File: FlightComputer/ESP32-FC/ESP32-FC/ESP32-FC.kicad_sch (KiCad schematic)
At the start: 19 parts, among them J1 USB_C_Receptacle_USB2.0_16P, U1 ESP32-S3-WROOM-1, U2 AP2112K-3.3, U3 ICP-20100, U4 ICM-42670-P

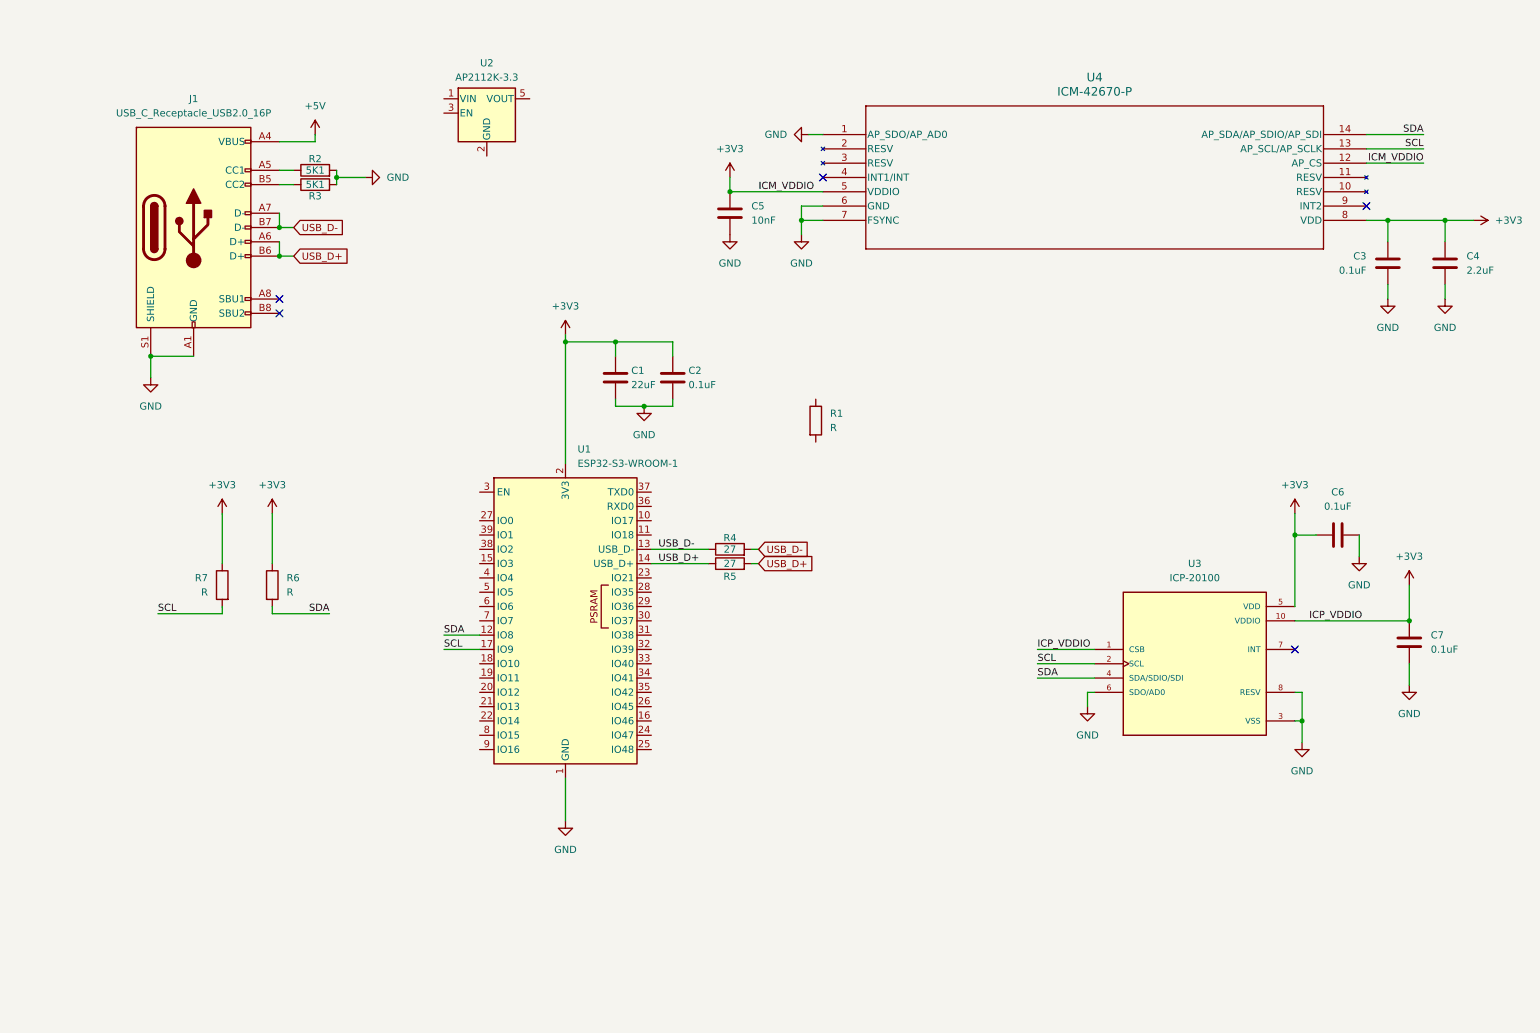
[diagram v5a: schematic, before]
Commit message: Updated power architecture
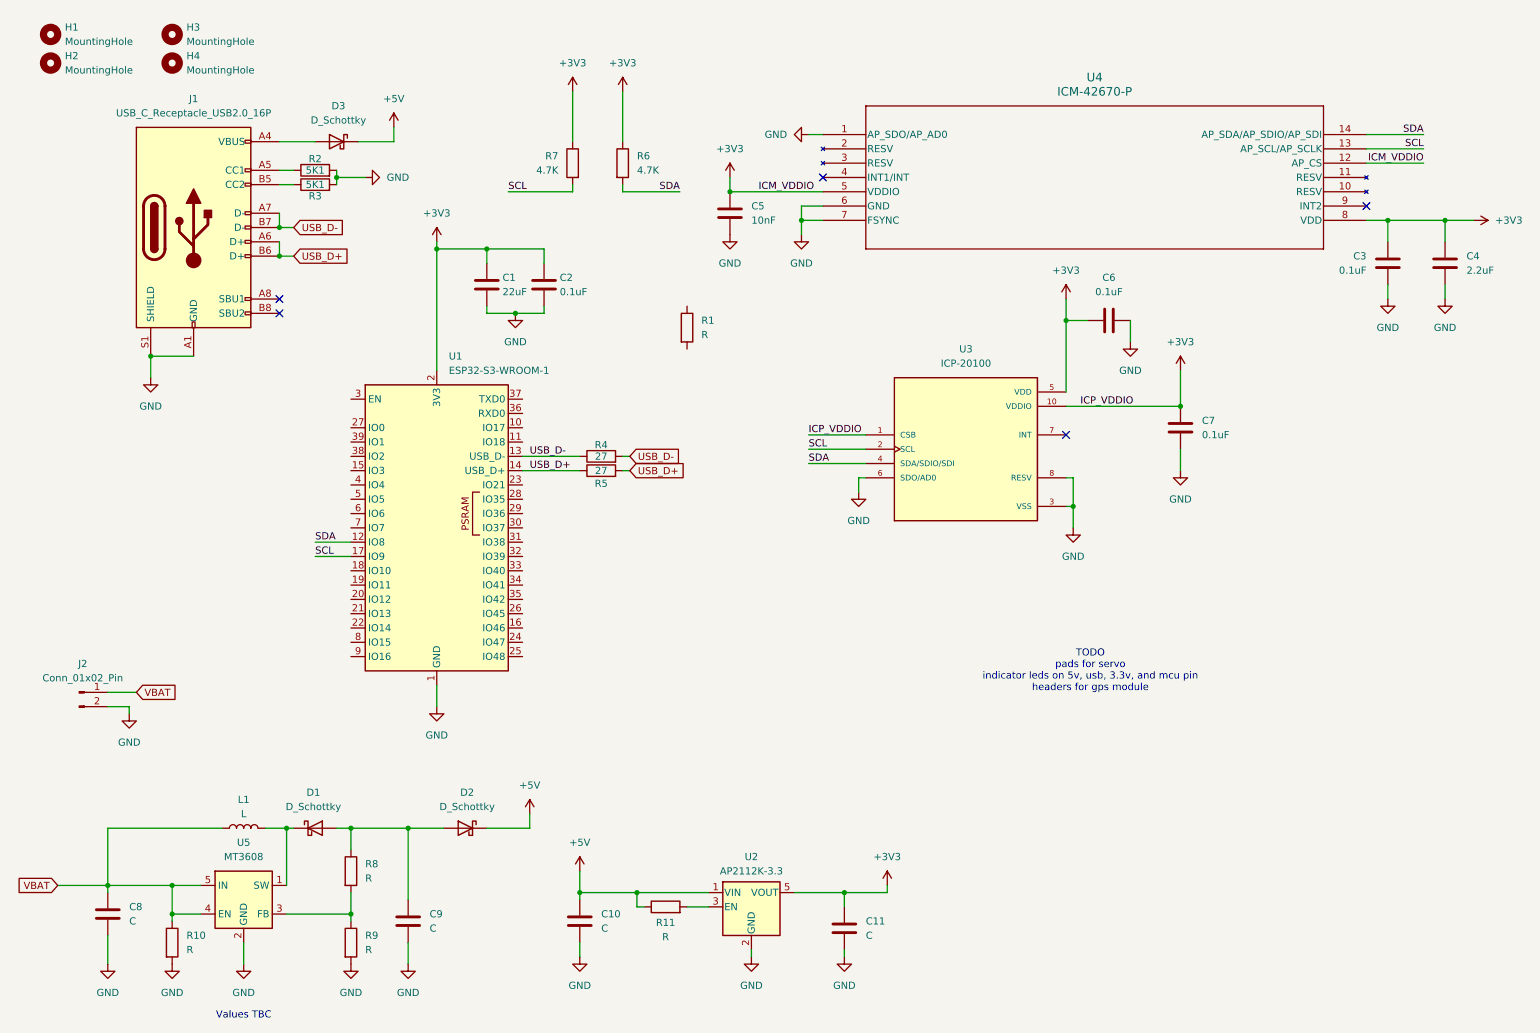
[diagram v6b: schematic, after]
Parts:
- added C10, C11, C8, C9: C, symbol Device:C
- added D1, D2, D3: D_Schottky, symbol Device:D_Schottky
- added H1, H2, H3, H4: MountingHole, symbol Mechanical:MountingHole
- added J2: Conn_01x02_Pin, symbol Connector:Conn_01x02_Pin
- added L1: L, symbol Device:L
- added R10, R11, R8, R9: R, symbol Device:R
- added U5: MT3608, Package_TO_SOT_SMD:SOT-23-6, symbol Regulator_Switching:MT3608
- R6, R7: value R -> 4.7K
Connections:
- net +3V3: now also U2.5 (VOUT), C11.1
- net +5V: now also U2.1 (VIN), C10.1, D2.1 (K), D3.1 (K), R11.1; no longer J1.A4 (VBUS), J1.A9 (VBUS), J1.B4 (VBUS), J1.B9 (VBUS)
- net GND: now also U2.2 (GND), C10.2, C11.2, C8.2, C9.2, J2.2 (Pin_2), R10.2, R9.2, U5.2 (GND)
- net at U2.3 (EN): now also R11.2
- new net: D3.2 (A), J1.A4 (VBUS), J1.A9 (VBUS), J1.B4 (VBUS), J1.B9 (VBUS)
- new net: D1.1 (K), L1.2, U5.1 (SW)
- new net: R8.2, R9.1, U5.3 (FB)
- new net: C9.1, D1.2 (A), D2.2 (A), R8.1
- new net VBAT: C8.1, J2.1 (Pin_1), L1.1, R10.1, U5.4 (EN), U5.5 (IN)
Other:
- note added: "TODO pads for servo indicator leds on 5v, usb, 3.3v, and mcu pin headers for gps module"
- note added: "Values TBC"
- moved on the sheet: C1, C2, C6, C7, R1, R4, R5, R6, R7, U1, U2, U3

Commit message: Servo + LEDs
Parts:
- added D4, D5, D6, D7: LED, symbol Device:LED
- added J3: Conn_01x04_Pin, symbol Connector:Conn_01x04_Pin
- added J4, J5: Conn_01x03_Pin, symbol Connector:Conn_01x03_Pin
- added R12, R13, R14, R15: R, symbol Device:R
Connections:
- net +3V3: now also D6.2 (A), J3.4 (Pin_4)
- net +5V: now also D5.2 (A), J4.2 (Pin_2), J5.2 (Pin_2), R12.1
- net GND: now also D4.1 (K), J3.1 (Pin_1), J4.1 (Pin_1), J5.1 (Pin_1), R13.1, R14.1, R15.1
- net ESP_TX: now reaches U1.10 (IO17)
- net ESP_TX: now also J3.3 (Pin_3)
- net ESP_RX: now reaches U1.11 (IO18)
- net ESP_RX: now also J3.2 (Pin_2)
- net SERVO2: now reaches U1.22 (IO14)
- net SERVO2: now also J5.3 (Pin_3)
- net at U1.25 (IO48): now also D7.2 (A)
- net SERVO1: now reaches U1.39 (IO1)
- net SERVO1: now also J4.3 (Pin_3)
- new net: D4.2 (A), R12.2
- new net: D6.1 (K), R14.2
- new net: D7.1 (K), R15.2
- new net: D5.1 (K), R13.2
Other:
- note added: "TODO esp32 boot config"
- note removed: "TODO pads for servo indicator leds on 5v, usb, 3.3v, and mcu pin headers for gps module"
- moved on the sheet: C10, C11, R11, R6, R7, U2

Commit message: Boot Config
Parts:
- added SW1: BOOT, symbol Switch:SW_Push
- added SW2: RESET, symbol Switch:SW_Push
- R6, R7: value 4.7K -> 4K7
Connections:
- net +3V3: now also R15.1
- net GND: now also R1.2, SW1.1, SW2.1; no longer R15.1
- net at U1.27 (IO0): now also SW1.2
- net EN: now reaches U1.3 (EN)
- net EN: now also R15.2, SW2.2
- net at R1.1: now also D7.1 (K)
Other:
- note removed: "TODO esp32 boot config"
- moved on the sheet: C1, C2, C3, C4, C5, C6, C7, D4, J2, J3, J4, J5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
